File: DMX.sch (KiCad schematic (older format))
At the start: 7 parts, among them U10 ST485CDR

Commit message: Changed the 5V-Regulator
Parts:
- C30: symbol C_Small -> device:C_Small
- JP2: symbol Jumper_NC_Small -> device:Jumper_NC_Small
- R22, R23, R24, R25: symbol R -> device:R
- U10: symbol MAX485E -> interface:MAX485E
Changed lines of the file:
@@
-EESchema Schematic File Version 2
-LIBS:power
-LIBS:device
-LIBS:switches
-LIBS:transistors
-LIBS:conn
-LIBS:linear
-LIBS:regul
-LIBS:74xx
-LIBS:analog_switches
-LIBS:texas
-LIBS:interface
-LIBS:philips
-LIBS:cypress
-LIBS:siliconi
-LIBS:opto
-LIBS:contrib
-LIBS:stm32s
-LIBS:transceiver
-LIBS:switchingR
-LIBS:ledDriver
-LIBS:jacks
-LIBS:sensors
+EESchema Schematic File Version 4
 LIBS:Hardware-cache
-EELAYER 25 0
+EELAYER 26 0
 EELAYER END
 $Descr A4 11693 8268
@@
 RS485-Transceiver
 $Comp
-L MAX485E U10
+L interface:MAX485E U10
 U 1 1 5A8476FC
 P 2200 2150
@@
 $EndComp
 $Comp
-L C_Small C30
+L device:C_Small C30
 U 1 1 5A847703
 P 2400 1400
@@
 $EndComp
 $Comp
-L GND #PWR084
+L power:GND #PWR084
 U 1 1 5A84770A
 P 2600 1450
@@
 $EndComp
 $Comp
-L +5V #PWR085
+L power:+5V #PWR085
 U 1 1 5A847710
 P 2200 1300
@@
 $EndComp
 $Comp
-L GND #PWR086
+L power:GND #PWR086
 U 1 1 5A847716
 P 2200 2900
@@
 $EndComp
 $Comp
-L R R22
+L device:R R22
 U 1 1 5A84771C
 P 1050 2250
@@
 $EndComp
 $Comp
-L R R24
+L device:R R24
 U 1 1 5A847723
 P 1050 2650
@@
 $EndComp
 $Comp
-L GND #PWR087
+L power:GND #PWR087
 U 1 1 5A84772A
 P 1050 2900
@@
 $EndComp
 $Comp
-L R R25
+L device:R R25
 U 1 1 5A847733
 P 1750 2650
@@
 UART_SE pulled high while sending
 $Comp
-L R R23
+L device:R R23
 U 1 1 5A847744
 P 3100 2400
@@
 $EndComp
 $Comp
-L Jumper_NC_Small JP2
+L device:Jumper_NC_Small JP2
 U 1 1 5A84774B
 P 2800 2400

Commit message: Minor Bugfixes
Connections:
- wire segments 22 -> 27
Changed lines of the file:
@@
 	2600 1400 2600 1450
 Wire Wire Line
-	2200 1300 2200 1650
+	2200 1300 2200 1400
 Wire Wire Line
 	2200 1400 2300 1400
@@
 Connection ~ 2200 1400
 Wire Wire Line
-	2200 2750 2200 2900
+	2200 2750 2200 2850
 Wire Wire Line
-	1050 2400 1050 2500
+	1050 2400 1050 2450
 Wire Wire Line
 	1050 2100 1050 2050
@@
 	2600 2050 3250 2050
 Wire Wire Line
-	2650 2350 2650 3150
+	2650 2350 2650 2400
 Wire Wire Line
-	3250 2050 3250 3150
+	3250 2050 3250 2400
 Wire Wire Line
 	2650 2350 2600 2350
@@
 Text HLabel 3250 3150 3    60   Input ~ 0
 DMX_B
+Wire Wire Line
+	2200 1400 2200 1650
+Wire Wire Line
+	1050 2450 1050 2500
+Wire Wire Line
+	2200 2850 2200 2900
+Wire Wire Line
+	2650 2400 2650 3150
+Wire Wire Line
+	3250 2400 3250 3150
 $EndSCHEMATC

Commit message: Updated to the new libraries
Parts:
- C30: symbol device:C_Small -> Device:C_Small
- JP2: symbol device:Jumper_NC_Small -> Device:Jumper_NC_Small
- R20: renamed from R22; symbol device:R -> Device:R
- R21: renamed from R24; symbol device:R -> Device:R
- R22: renamed from R25; symbol device:R -> Device:R
- R23: symbol device:R -> Device:R
- U10: symbol interface:MAX485E -> Interface_UART:MAX485E
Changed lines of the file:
@@
 RS485-Transceiver
 $Comp
-L interface:MAX485E U10
+L Interface_UART:MAX485E U10
 U 1 1 5A8476FC
 P 2200 2150
@@
 $EndComp
 $Comp
-L device:C_Small C30
+L Device:C_Small C30
 U 1 1 5A847703
 P 2400 1400
@@
 $EndComp
 $Comp
-L power:GND #PWR084
+L power:GND #PWR082
 U 1 1 5A84770A
 P 2600 1450
-F 0 "#PWR084" H 2600 1200 50  0001 C CNN
+F 0 "#PWR082" H 2600 1200 50  0001 C CNN
 F 1 "GND" H 2600 1300 50  0000 C CNN
 F 2 "" H 2600 1450 50  0001 C CNN
@@
 $EndComp
 $Comp
-L power:+5V #PWR085
+L power:+5V #PWR080
 U 1 1 5A847710
 P 2200 1300
-F 0 "#PWR085" H 2200 1150 50  0001 C CNN
+F 0 "#PWR080" H 2200 1150 50  0001 C CNN
 F 1 "+5V" H 2200 1440 50  0000 C CNN
 F 2 "" H 2200 1300 50  0001 C CNN
@@
 $EndComp
 $Comp
-L power:GND #PWR086
+L power:GND #PWR081
 U 1 1 5A847716
 P 2200 2900
-F 0 "#PWR086" H 2200 2650 50  0001 C CNN
+F 0 "#PWR081" H 2200 2650 50  0001 C CNN
 F 1 "GND" H 2200 2750 50  0000 C CNN
 F 2 "" H 2200 2900 50  0001 C CNN
@@
 $EndComp
 $Comp
-L device:R R22
+L Device:R R20
 U 1 1 5A84771C
 P 1050 2250
-F 0 "R22" V 1130 2250 50  0000 C CNN
+F 0 "R20" V 1130 2250 50  0000 C CNN
 F 1 "6k6" V 1050 2250 50  0000 C CNN
 F 2 "Resistors_SMD:R_0603" V 980 2250 50  0001 C CNN
@@
 $EndComp
 $Comp
-L device:R R24
+L Device:R R21
 U 1 1 5A847723
 P 1050 2650
-F 0 "R24" V 1130 2650 50  0000 C CNN
+F 0 "R21" V 1130 2650 50  0000 C CNN
 F 1 "10k" V 1050 2650 50  0000 C CNN
 F 2 "Resistors_SMD:R_0603" V 980 2650 50  0001 C CNN
@@
 $EndComp
 $Comp
-L power:GND #PWR087
+L power:GND #PWR079
 U 1 1 5A84772A
 P 1050 2900
-F 0 "#PWR087" H 1050 2650 50  0001 C CNN
+F 0 "#PWR079" H 1050 2650 50  0001 C CNN
 F 1 "GND" H 1050 2750 50  0000 C CNN
 F 2 "" H 1050 2900 50  0001 C CNN
@@
 $EndComp
 $Comp
-L device:R R25
+L Device:R R22
 U 1 1 5A847733
 P 1750 2650
-F 0 "R25" V 1830 2650 50  0000 C CNN
+F 0 "R22" V 1830 2650 50  0000 C CNN
 F 1 "10k" V 1750 2650 50  0000 C CNN
 F 2 "Resistors_SMD:R_0603" V 1680 2650 50  0001 C CNN
@@
 UART_SE pulled high while sending
 $Comp
-L device:R R23
+L Device:R R23
 U 1 1 5A847744
 P 3100 2400
@@
 $EndComp
 $Comp
-L device:Jumper_NC_Small JP2
+L Device:Jumper_NC_Small JP2
 U 1 1 5A84774B
 P 2800 2400

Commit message: Added Component-Associations (about 10% remaining)
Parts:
- C30: Buy (none) -> https://www.digikey.com/product-detail/en/kemet/C0603C104M5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
- R20: value 6k6 -> 6k8; Buy (none) -> https://www.digikey.com/product-detail/en/yageo/RC0603JR-07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
- R21, R22: Buy (none) -> https://www.digikey.com/product-detail/en/yageo/RC0603FR-07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
- R23: footprint Resistors_SMD:R_0603 -> Resistors_SMD:R_1206; Buy (none) -> https://www.digikey.com/product-detail/en/yageo/RC1206FR-07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
- U10: Buy (none) -> https://www.digikey.com/product-detail/en/stmicroelectronic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
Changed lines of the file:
@@
 F 2 "Housings_SOIC:SOIC-8_3.9x4.9mm_Pitch1.27mm" H 2200 1450 50  0001 C CNN
 F 3 "http://www.st.com/content/ccc/resource/technical/document/datasheet/4b/81/a8/cd/8a/72/47/82/CD00002183.pdf/files/CD00002183.pdf/jcr:content/translations/en.CD00002183.pdf" H 2200 2200 50  0001 C CNN
+F 4 "https://www.digikey.com/product-detail/en/stmicroelectronics/ST485CDR/497-3734-1-ND/686452" H 2200 2150 50  0001 C CNN "Buy"
 	1    2200 2150
 	1    0    0    -1
@@
 F 2 "Capacitors_SMD:C_0603" H 2400 1400 50  0001 C CNN
 F 3 "" H 2400 1400 50  0001 C CNN
+F 4 "https://www.digikey.com/product-detail/en/kemet/C0603C104M5RACTU/399-7845-1-ND/3471568" V 2400 1400 50  0001 C CNN "Buy"
 	1    2400 1400
 	0    1    1    0
@@
 P 1050 2250
 F 0 "R20" V 1130 2250 50  0000 C CNN
-F 1 "6k6" V 1050 2250 50  0000 C CNN
+F 1 "6k8" V 1050 2250 50  0000 C CNN
 F 2 "Resistors_SMD:R_0603" V 980 2250 50  0001 C CNN
 F 3 "" H 1050 2250 50  0001 C CNN
+F 4 "https://www.digikey.com/product-detail/en/yageo/RC0603JR-076K8L/311-6.8KGRCT-ND/729760" V 1050 2250 50  0001 C CNN "Buy"
 	1    1050 2250
 	1    0    0    -1
@@
 F 2 "Resistors_SMD:R_0603" V 980 2650 50  0001 C CNN
 F 3 "" H 1050 2650 50  0001 C CNN
+F 4 "https://www.digikey.com/product-detail/en/yageo/RC0603FR-0710KL/311-10.0KHRCT-ND/729827" V 1050 2650 50  0001 C CNN "Buy"
 	1    1050 2650
 	1    0    0    -1
@@
 F 2 "Resistors_SMD:R_0603" V 1680 2650 50  0001 C CNN
 F 3 "" H 1750 2650 50  0001 C CNN
+F 4 "https://www.digikey.com/product-detail/en/yageo/RC0603FR-0710KL/311-10.0KHRCT-ND/729827" V 1750 2650 50  0001 C CNN "Buy"
 	1    1750 2650
 	1    0    0    -1
@@
 F 0 "R23" V 3180 2400 50  0000 C CNN
 F 1 "120" V 3100 2400 50  0000 C CNN
-F 2 "Resistors_SMD:R_0603" V 3030 2400 50  0001 C CNN
+F 2 "Resistors_SMD:R_1206" V 3030 2400 50  0001 C CNN
 F 3 "" H 3100 2400 50  0001 C CNN
+F 4 "https://www.digikey.com/product-detail/en/yageo/RC1206FR-07120RL/311-120FRCT-ND/731470" V 3100 2400 50  0001 C CNN "Buy"
 	1    3100 2400
 	0    1    1    0

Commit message: Minor changes to layout and component association
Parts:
- C30: Buy https://www.digikey.com/product-detail/en/kemet/C0603C104M5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 -> https://www.digikey.com/product-detail/en/kemet/C0603C104K3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
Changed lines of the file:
@@
 F 2 "Capacitors_SMD:C_0603" H 2400 1400 50  0001 C CNN
 F 3 "" H 2400 1400 50  0001 C CNN
-F 4 "https://www.digikey.com/product-detail/en/kemet/C0603C104M5RACTU/399-7845-1-ND/3471568" V 2400 1400 50  0001 C CNN "Buy"
+F 4 "https://www.digikey.com/product-detail/en/kemet/C0603C104K3RACTU/399-1281-1-ND/416057" V 2400 1400 50  0001 C CNN "Buy"
 	1    2400 1400
 	0    1    1    0

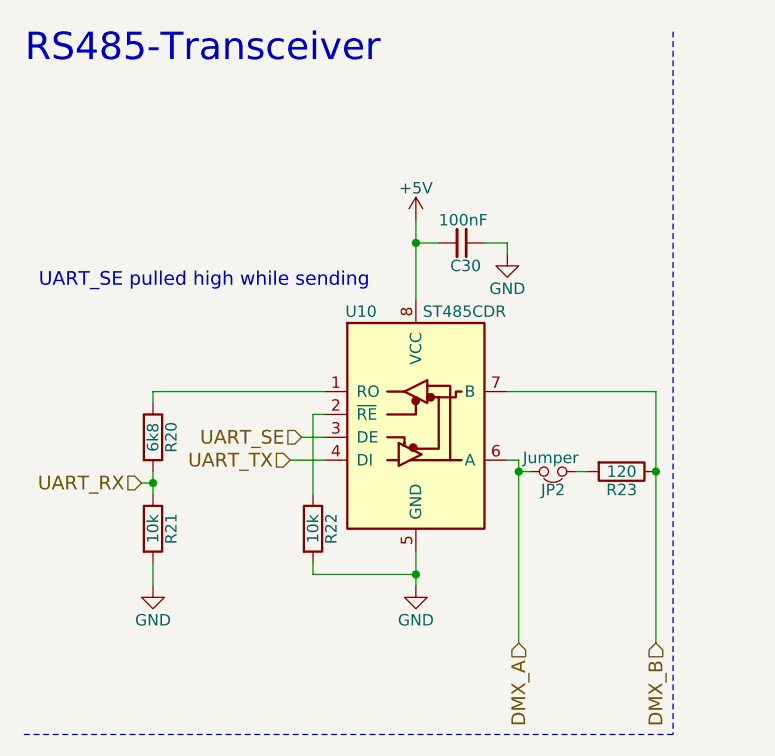
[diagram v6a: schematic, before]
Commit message: Added about 8% of the remaining components
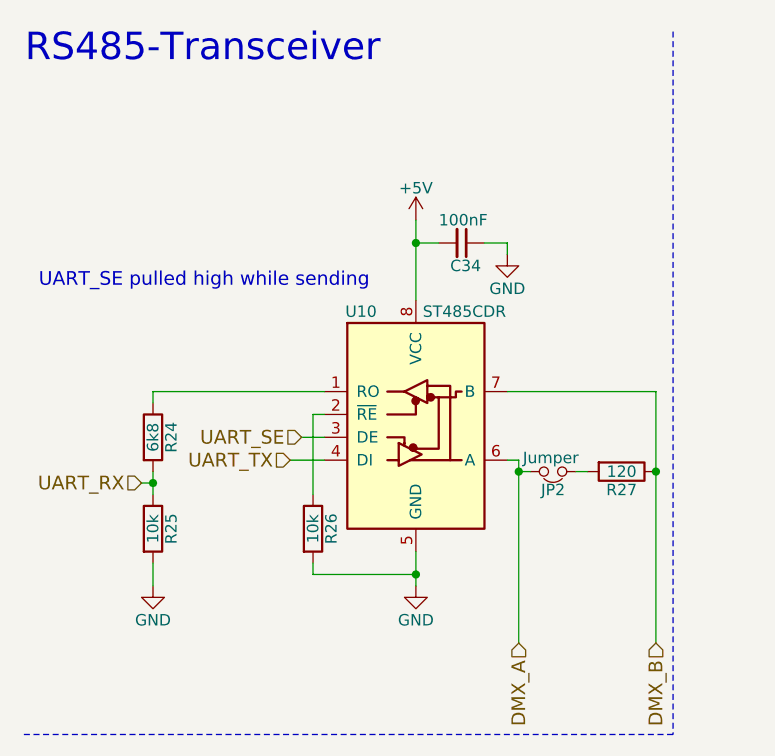
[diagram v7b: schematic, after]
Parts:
- renumbered C30 to C34, R20 to R24, R21 to R25, R22 to R26, R23 to R27
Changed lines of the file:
@@
 $EndComp
 $Comp
-L Device:C_Small C30
+L Device:C_Small C34
 U 1 1 5A847703
 P 2400 1400
-F 0 "C30" V 2500 1350 50  0000 L CNN
+F 0 "C34" V 2500 1350 50  0000 L CNN
 F 1 "100nF" V 2300 1300 50  0000 L CNN
 F 2 "Capacitors_SMD:C_0603" H 2400 1400 50  0001 C CNN
@@
 $EndComp
 $Comp
-L power:GND #PWR085
+L power:GND #PWR088
 U 1 1 5A84770A
 P 2600 1450
-F 0 "#PWR085" H 2600 1200 50  0001 C CNN
+F 0 "#PWR088" H 2600 1200 50  0001 C CNN
 F 1 "GND" H 2600 1300 50  0000 C CNN
 F 2 "" H 2600 1450 50  0001 C CNN
@@
 $EndComp
 $Comp
-L power:+5V #PWR083
+L power:+5V #PWR086
 U 1 1 5A847710
 P 2200 1300
-F 0 "#PWR083" H 2200 1150 50  0001 C CNN
+F 0 "#PWR086" H 2200 1150 50  0001 C CNN
 F 1 "+5V" H 2200 1440 50  0000 C CNN
 F 2 "" H 2200 1300 50  0001 C CNN
@@
 $EndComp
 $Comp
-L power:GND #PWR084
+L power:GND #PWR087
 U 1 1 5A847716
 P 2200 2900
-F 0 "#PWR084" H 2200 2650 50  0001 C CNN
+F 0 "#PWR087" H 2200 2650 50  0001 C CNN
 F 1 "GND" H 2200 2750 50  0000 C CNN
 F 2 "" H 2200 2900 50  0001 C CNN
@@
 $EndComp
 $Comp
-L Device:R R20
+L Device:R R24
 U 1 1 5A84771C
 P 1050 2250
-F 0 "R20" V 1130 2250 50  0000 C CNN
+F 0 "R24" V 1130 2250 50  0000 C CNN
 F 1 "6k8" V 1050 2250 50  0000 C CNN
 F 2 "Resistors_SMD:R_0603" V 980 2250 50  0001 C CNN
@@
 $EndComp
 $Comp
-L Device:R R21
+L Device:R R25
 U 1 1 5A847723
 P 1050 2650
-F 0 "R21" V 1130 2650 50  0000 C CNN
+F 0 "R25" V 1130 2650 50  0000 C CNN
 F 1 "10k" V 1050 2650 50  0000 C CNN
 F 2 "Resistors_SMD:R_0603" V 980 2650 50  0001 C CNN
@@
 $EndComp
 $Comp
-L power:GND #PWR082
+L power:GND #PWR085
 U 1 1 5A84772A
 P 1050 2900
-F 0 "#PWR082" H 1050 2650 50  0001 C CNN
+F 0 "#PWR085" H 1050 2650 50  0001 C CNN
 F 1 "GND" H 1050 2750 50  0000 C CNN
 F 2 "" H 1050 2900 50  0001 C CNN
@@
 $EndComp
 $Comp
-L Device:R R22
+L Device:R R26
 U 1 1 5A847733
 P 1750 2650
-F 0 "R22" V 1830 2650 50  0000 C CNN
+F 0 "R26" V 1830 2650 50  0000 C CNN
 F 1 "10k" V 1750 2650 50  0000 C CNN
 F 2 "Resistors_SMD:R_0603" V 1680 2650 50  0001 C CNN
@@
 UART_SE pulled high while sending
 $Comp
-L Device:R R23
+L Device:R R27
 U 1 1 5A847744
 P 3100 2400
-F 0 "R23" V 3180 2400 50  0000 C CNN
+F 0 "R27" V 3180 2400 50  0000 C CNN
 F 1 "120" V 3100 2400 50  0000 C CNN
 F 2 "Resistors_SMD:R_1206" V 3030 2400 50  0001 C CNN

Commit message: Switch to new kicad footprint library
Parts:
- C34: footprint Capacitors_SMD:C_0603 -> Capacitor_SMD:C_0603_1608Metric
- JP2: footprint Socket_Strips:Socket_Strip_Straight_2x01_Pitch2.54mm -> Connector_PinHeader_2.54mm:PinHeader_2x01_P2.54mm_Vertical
- R24, R25, R26: footprint Resistors_SMD:R_0603 -> Resistor_SMD:R_0603_1608Metric
- R27: footprint Resistors_SMD:R_1206 -> Resistor_SMD:R_1206_3216Metric
- U10: footprint Housings_SOIC:SOIC-8_3.9x4.9mm_Pitch1.27mm -> Package_SO:SOIC-8_3.9x4.9mm_P1.27mm
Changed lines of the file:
@@
 F 0 "U10" H 1960 2600 50  0000 C CNN
 F 1 "ST485CDR" H 2230 2600 50  0000 L CNN
-F 2 "Housings_SOIC:SOIC-8_3.9x4.9mm_Pitch1.27mm" H 2200 1450 50  0001 C CNN
+F 2 "Package_SO:SOIC-8_3.9x4.9mm_P1.27mm" H 2200 1450 50  0001 C CNN
 F 3 "http://www.st.com/content/ccc/resource/technical/document/datasheet/4b/81/a8/cd/8a/72/47/82/CD00002183.pdf/files/CD00002183.pdf/jcr:content/translations/en.CD00002183.pdf" H 2200 2200 50  0001 C CNN
 F 4 "https://www.digikey.com/product-detail/en/stmicroelectronics/ST485CDR/497-3734-1-ND/686452" H 2200 2150 50  0001 C CNN "Buy"
@@
 F 0 "C34" V 2500 1350 50  0000 L CNN
 F 1 "100nF" V 2300 1300 50  0000 L CNN
-F 2 "Capacitors_SMD:C_0603" H 2400 1400 50  0001 C CNN
+F 2 "Capacitor_SMD:C_0603_1608Metric" H 2400 1400 50  0001 C CNN
 F 3 "" H 2400 1400 50  0001 C CNN
 F 4 "https://www.digikey.com/product-detail/en/kemet/C0603C104K3RACTU/399-1281-1-ND/416057" V 2400 1400 50  0001 C CNN "Buy"
@@
 F 0 "R24" V 1130 2250 50  0000 C CNN
 F 1 "6k8" V 1050 2250 50  0000 C CNN
-F 2 "Resistors_SMD:R_0603" V 980 2250 50  0001 C CNN
+F 2 "Resistor_SMD:R_0603_1608Metric" V 980 2250 50  0001 C CNN
 F 3 "" H 1050 2250 50  0001 C CNN
 F 4 "https://www.digikey.com/product-detail/en/yageo/RC0603JR-076K8L/311-6.8KGRCT-ND/729760" V 1050 2250 50  0001 C CNN "Buy"
@@
 F 0 "R25" V 1130 2650 50  0000 C CNN
 F 1 "10k" V 1050 2650 50  0000 C CNN
-F 2 "Resistors_SMD:R_0603" V 980 2650 50  0001 C CNN
+F 2 "Resistor_SMD:R_0603_1608Metric" V 980 2650 50  0001 C CNN
 F 3 "" H 1050 2650 50  0001 C CNN
 F 4 "https://www.digikey.com/product-detail/en/yageo/RC0603FR-0710KL/311-10.0KHRCT-ND/729827" V 1050 2650 50  0001 C CNN "Buy"
@@
 F 0 "R26" V 1830 2650 50  0000 C CNN
 F 1 "10k" V 1750 2650 50  0000 C CNN
-F 2 "Resistors_SMD:R_0603" V 1680 2650 50  0001 C CNN
+F 2 "Resistor_SMD:R_0603_1608Metric" V 1680 2650 50  0001 C CNN
 F 3 "" H 1750 2650 50  0001 C CNN
 F 4 "https://www.digikey.com/product-detail/en/yageo/RC0603FR-0710KL/311-10.0KHRCT-ND/729827" V 1750 2650 50  0001 C CNN "Buy"
@@
 F 0 "R27" V 3180 2400 50  0000 C CNN
 F 1 "120" V 3100 2400 50  0000 C CNN
-F 2 "Resistors_SMD:R_1206" V 3030 2400 50  0001 C CNN
+F 2 "Resistor_SMD:R_1206_3216Metric" V 3030 2400 50  0001 C CNN
 F 3 "" H 3100 2400 50  0001 C CNN
 F 4 "https://www.digikey.com/product-detail/en/yageo/RC1206FR-07120RL/311-120FRCT-ND/731470" V 3100 2400 50  0001 C CNN "Buy"
@@
 F 0 "JP2" H 2800 2480 50  0000 C CNN
 F 1 "Jumper" H 2810 2340 50  0000 C CNN
-F 2 "Socket_Strips:Socket_Strip_Straight_2x01_Pitch2.54mm" H 2800 2400 50  0001 C CNN
+F 2 "Connector_PinHeader_2.54mm:PinHeader_2x01_P2.54mm_Vertical" H 2800 2400 50  0001 C CNN
 F 3 "" H 2800 2400 50  0001 C CNN
 	1    2800 2400
